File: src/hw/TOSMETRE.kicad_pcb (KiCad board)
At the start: 2 copper layers, 203.2 x 50.8 mm, 15 parts, among them J1 +, J2 -, J3 Conn_01x01, J4 Conn_01x01, U1 16F88_SSOP, U2 L7805, Y1 Crystal

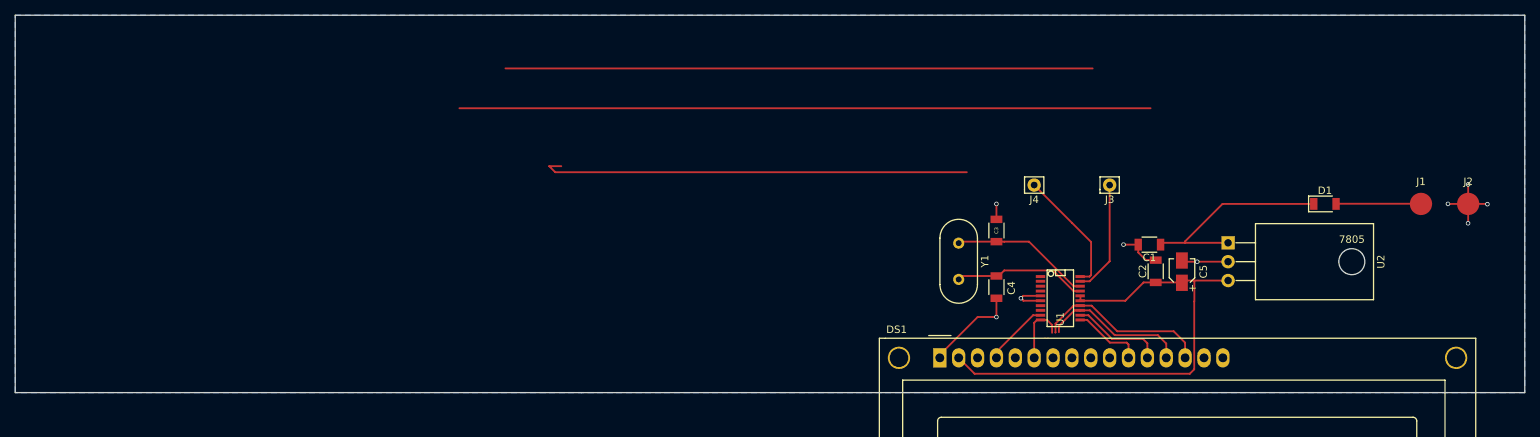
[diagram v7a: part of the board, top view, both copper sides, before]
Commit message: MODIF EN COURS AVEC CONNECTEUR PROGRAMMATION  LA PRISE DE TETE A VENIR ........................
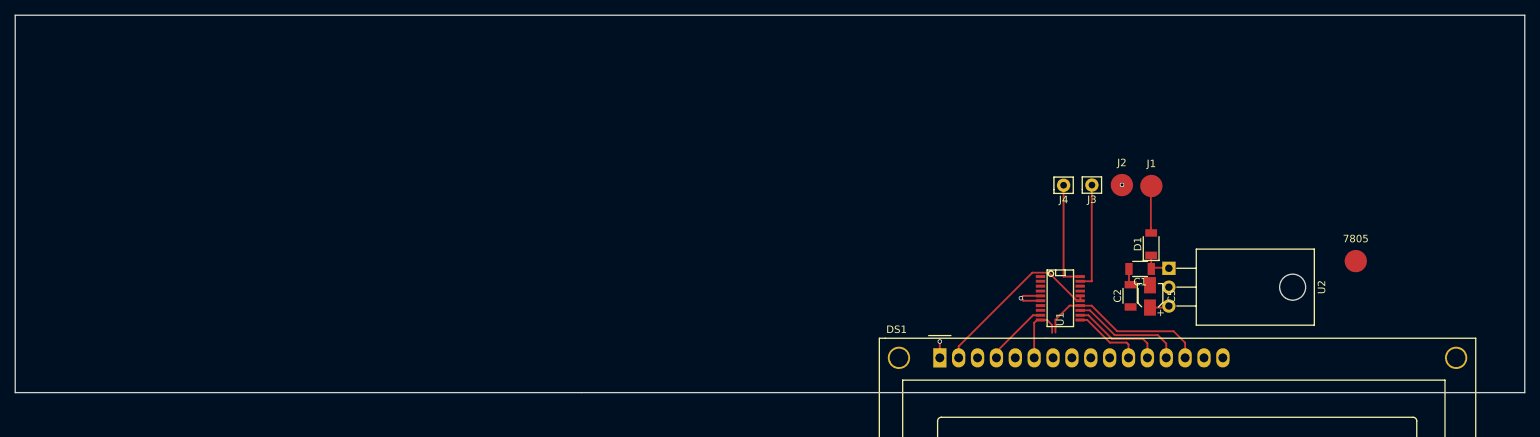
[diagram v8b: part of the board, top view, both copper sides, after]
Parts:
- removed C3, C4: C, Capacitors_SMD:C_1206
- removed Y1: Crystal, Crystals:Crystal_HC49-U_Vertical
- J1: value + -> Conn_01x01_Female
- J2: value - -> Conn_01x01_Female
- moved J2 46.7 mm to (207.4, 127.0)
- moved J1 36.4 mm to (211.4, 127.1)
- moved D1 24.0 mm to (211.3, 135.0), turned to 90 degrees
- moved U2 8.68 mm to (213.7, 138.2)
- moved C5 5.44 mm to (211.2, 142.0)
- moved C2 4.73 mm to (208.6, 141.9)
- moved J4 3.96 mm to (199.5, 127.0)
- moved C1 3.50 mm to (209.8, 138.3)
- moved J3 2.39 mm to (203.4, 127.0)
- moved 7805 0.54 mm to (238.9, 137.2)
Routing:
- net (no net): track 230.3 -> 0.00 mm
- net Net-(C2-Pad1): track 66.5 -> 27.3 mm
- net GNDREF: track 43.0 -> 10.7 mm, vias 9 -> 3
- net Net-(C1-Pad1): track 29.4 -> 5.77 mm
- net Net-(U1-Pad18): track 18.9 -> 0.00 mm
- net Net-(U1-Pad17): track 18.0 -> 0.00 mm
- net Net-(D1-Pad2): track 12.7 -> 6.23 mm
- net Net-(DS1-Pad13): track 19.5 -> 15.0 mm
- net Net-(J4-Pad1): track 16.9 -> 14.5 mm
- net Net-(J3-Pad1): track 15.3 -> 14.5 mm
- removed copper zone on B.Cu, net GNDREF
